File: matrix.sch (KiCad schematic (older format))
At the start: 46 parts

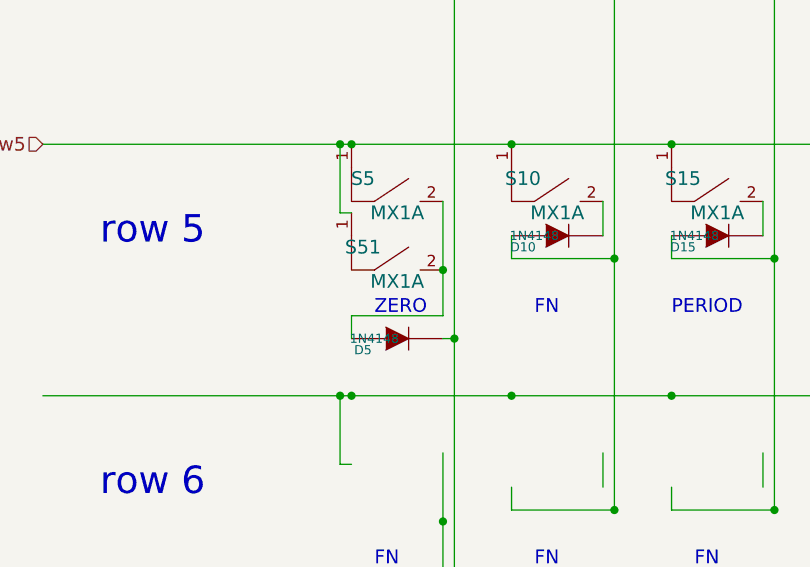
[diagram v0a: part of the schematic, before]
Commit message: fixed silkscreen
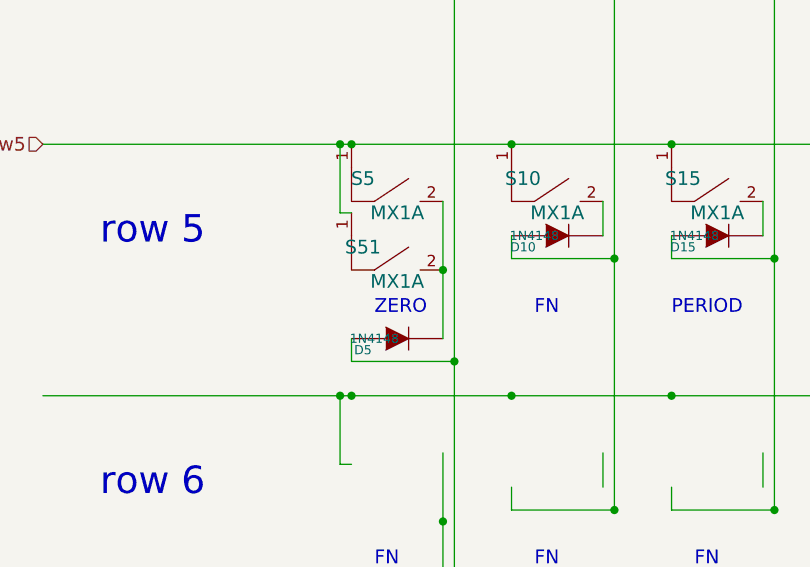
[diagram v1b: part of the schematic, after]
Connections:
- wire segments 98 -> 97
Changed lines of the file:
@@
-EESchema Schematic File Version 2  date 1/1/2014 1:44:05 PM
+EESchema Schematic File Version 2  date 1/1/2014 8:23:56 PM
 LIBS:power
 LIBS:mx1a-simple
@@
 LIBS:mcp23018
 LIBS:component
+LIBS:keyboard-cache
 EELAYER 27 0
 EELAYER END
@@
 Sheet 2 2
 Title "4x5 keypad"
-Date "17 dec 2013"
+Date "2 jan 2014"
 Rev "0.12.2"
 Comp "regack"
@@
 Connection ~ 4300 8600
 Wire Wire Line
-	3550 8350 3550 8850
+	3550 8350 3550 8950
 $Comp
 L MX1A S20
@@
 	1    0    0    -1
 $EndComp
-Wire Wire Line
-	3550 8850 3150 8850
-Wire Wire Line
-	3150 8850 3150 8950
-Wire Wire Line
-	3550 8950 3600 8950
-Connection ~ 3600 8950
 Connection ~ 3100 8100
 $Comp
@@
 Text Notes 7300 4600 0    120  ~ 0
 Resistor Value dependent upon LED value
+Wire Wire Line
+	3150 8950 3150 9050
+Wire Wire Line
+	3150 9050 3600 9050
+Connection ~ 3600 9050
 $EndSCHEMATC
